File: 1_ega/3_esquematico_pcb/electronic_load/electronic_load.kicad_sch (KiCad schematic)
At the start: 43 parts, among them J1 Encoder, J10 VCC, J11 LOAD, J12 FAN, J13 RTC_I2C, J2 LCD_I2C, J3 GND, J4 MOS_GATE, J5 Isense, J6 Vload_LPF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

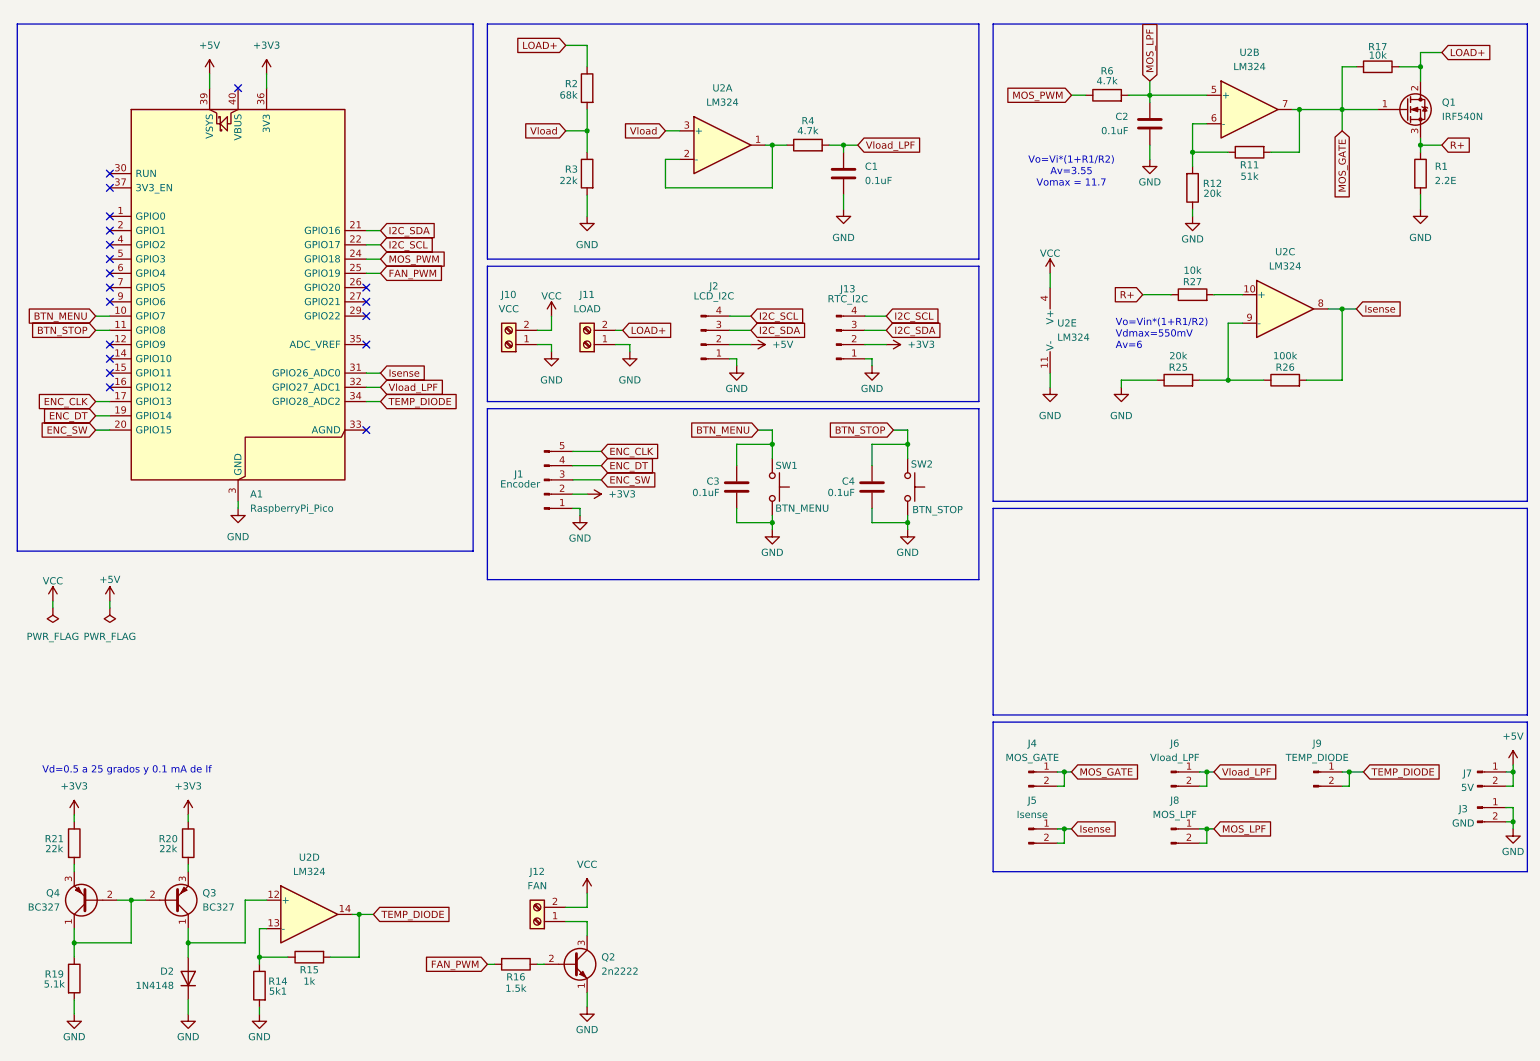
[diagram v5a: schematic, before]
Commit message: test version of i2c_guard
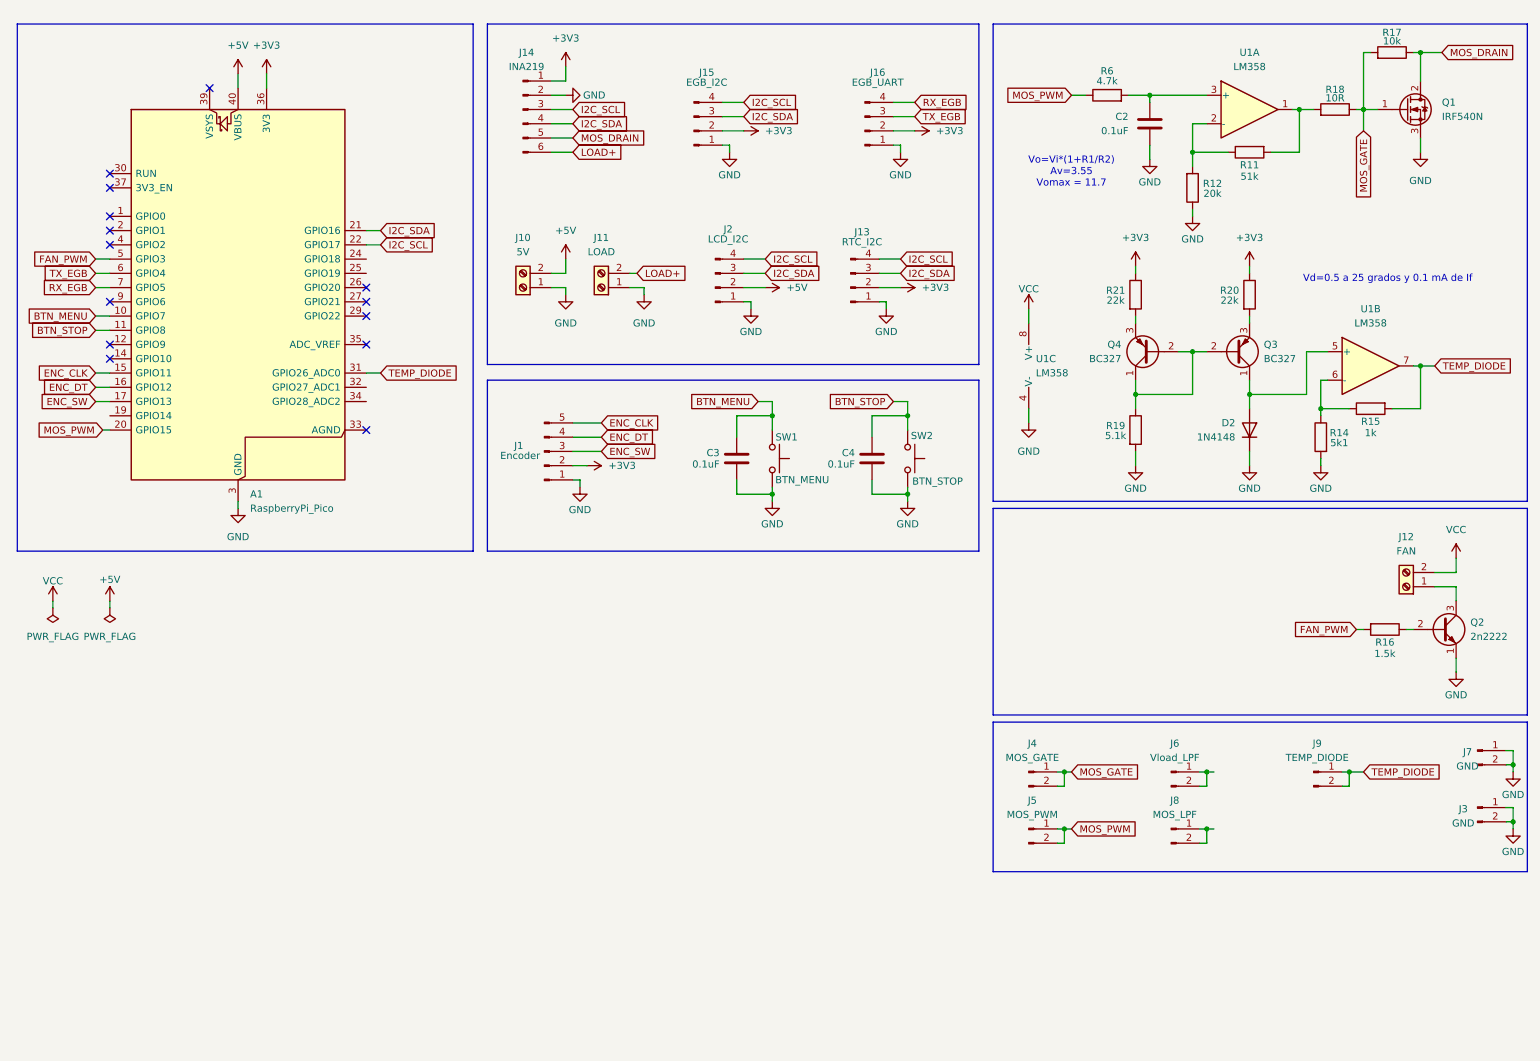
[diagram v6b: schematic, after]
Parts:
- removed C1: 0.1uF, Capacitor_THT:C_Disc_D3.4mm_W2.1mm_P2.50mm, symbol Device:C
- removed R1: 2.2E, Resistor_THT:R_Axial_Power_L25.0mm_W9.0mm_P27.94mm, symbol Device:R
- removed R2: 68k, Resistor_THT:R_Axial_DIN0207_L6.3mm_D2.5mm_P10.16mm_Horizontal, symbol Device:R
- removed R25: 20k, Resistor_THT:R_Axial_DIN0207_L6.3mm_D2.5mm_P10.16mm_Horizontal, symbol Device:R
- removed R26: 100k, Resistor_THT:R_Axial_DIN0207_L6.3mm_D2.5mm_P10.16mm_Horizontal, symbol Device:R
- removed R27: 10k, Resistor_THT:R_Axial_DIN0207_L6.3mm_D2.5mm_P10.16mm_Horizontal, symbol Device:R
- removed R3: 22k, Resistor_THT:R_Axial_DIN0207_L6.3mm_D2.5mm_P10.16mm_Horizontal, symbol Device:R
- removed R4: 4.7k, Resistor_THT:R_Axial_DIN0207_L6.3mm_D2.5mm_P10.16mm_Horizontal, symbol Device:R
- removed U2: LM324, symbol Amplifier_Operational:LM324
- added J14: INA219, Connector_PinSocket_2.54mm:PinSocket_1x06_P2.54mm_Vertical, symbol Connector:Conn_01x06_Pin
- added J15: EGB_I2C, Connector_PinSocket_2.54mm:PinSocket_1x04_P2.54mm_Vertical, symbol Connector:Conn_01x04_Pin
- added J16: EGB_UART, Connector_PinSocket_2.54mm:PinSocket_1x04_P2.54mm_Vertical, symbol Connector:Conn_01x04_Pin
- added R18: 10R, Resistor_THT:R_Axial_DIN0207_L6.3mm_D2.5mm_P10.16mm_Horizontal, symbol Device:R
- added U1: LM358, Package_DIP:DIP-8_W7.62mm_Socket_LongPads, symbol Amplifier_Operational:LM358
- J10: value VCC -> 5V
- J5: value Isense -> MOS_PWM
- J7: value 5V -> GND
- Q3, Q4: footprint Package_TO_SOT_THT:TO-92_Inline -> Package_TO_SOT_THT:TO-92_Inline_Wide
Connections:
- net R+ is gone; now on net GND: Q1.3 (S)
- net +3V3: now also J14.1 (Pin_1), J15.2 (Pin_2), J16.2 (Pin_2)
- net +5V: now also A1.40 (VBUS), J10.2 (Pin_2); no longer A1.39 (VSYS), J7.1 (Pin_1), J7.2 (Pin_2)
- net ENC_CLK: now also A1.15 (GPIO11); no longer A1.17 (GPIO13)
- net ENC_DT: now also A1.16 (GPIO12); no longer A1.19 (GPIO14)
- net ENC_SW: now also A1.17 (GPIO13); no longer A1.20 (GPIO15)
- net FAN_PWM: now also A1.5 (GPIO3); no longer A1.25 (GPIO19)
- net GND: now also J7.1 (Pin_1), J7.2 (Pin_2), J14.2 (Pin_2), J15.1 (Pin_1), J16.1 (Pin_1), U1.4 (V-)
- net I2C_SCL: now also J14.3 (Pin_3), J15.4 (Pin_4)
- net I2C_SDA: now also J14.4 (Pin_4), J15.3 (Pin_3)
- net LOAD+: now also J14.6 (Pin_6); no longer Q1.2 (D), R17.1
- net MOS_GATE: now also R18.1; no longer R11.2
- net MOS_PWM: now also A1.20 (GPIO15), J5.1 (Pin_1), J5.2 (Pin_2); no longer A1.24 (GPIO18)
- net TEMP_DIODE: now also A1.31 (GPIO26_ADC0), U1.7; no longer A1.34 (GPIO28_ADC2)
- net VCC: now also U1.8 (V+); no longer J10.2 (Pin_2)
- net at R11.1, R12.2: now also U1.2 (-)
- net at R14.1, R15.1: now also U1.6 (-)
- net at D2.2 (A), Q3.1 (C): now also U1.5 (+)
- net TX_EGB: now reaches A1.6 (GPIO4)
- net TX_EGB: now also J16.3 (Pin_3)
- net RX_EGB: now reaches A1.7 (GPIO5)
- net RX_EGB: now also J16.4 (Pin_4)
- removed net Isense: A1.31 (GPIO26_ADC0), J5.1 (Pin_1), J5.2 (Pin_2)
- net MOS_LPF: no longer names the net of C2.1, R6.2
- net MOS_LPF: now also U1.3 (+); no longer J8.1 (Pin_1), J8.2 (Pin_2)
- net Vload_LPF: no longer names the net of J6.1 (Pin_1), J6.2 (Pin_2)
- net Vload_LPF: no longer A1.32 (GPIO27_ADC1)
- new net: R11.2, R18.2, U1.1
- new net: J8.1 (Pin_1), J8.2 (Pin_2)
- new net MOS_DRAIN: J14.5 (Pin_5), Q1.2 (D), R17.1
- no-connect marks 19 -> 14
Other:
- note removed: "Vo=Vin*(1+R1/R2) Vdmax=550mV Av=6"
- moved on the sheet: C3, C4, D2, J1, J10, J11, J12, J13, J2, J7, Q2, Q3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

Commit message: feat: schematic and pcb full v1
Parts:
- removed J12: FAN, TerminalBlock_Phoenix:TerminalBlock_Phoenix_MKDS-1,5-2-5.08_1x02_P5.08mm_Horizontal, symbol Connector:Screw_Terminal_01x02
- removed J13: RTC_I2C, Connector_PinSocket_2.54mm:PinSocket_1x04_P2.54mm_Vertical, symbol Connector:Conn_01x04_Pin
- removed J15: EGB_I2C, Connector_PinSocket_2.54mm:PinSocket_1x04_P2.54mm_Vertical, symbol Connector:Conn_01x04_Pin
- removed J16: EGB_UART, Connector_PinSocket_2.54mm:PinSocket_1x04_P2.54mm_Vertical, symbol Connector:Conn_01x04_Pin
- removed J2: LCD_I2C, Connector_PinSocket_2.54mm:PinSocket_1x04_P2.54mm_Vertical, symbol Connector:Conn_01x04_Pin
- removed Q2: 2n2222, Package_TO_SOT_THT:TO-92L_Inline_Wide, symbol Transistor_BJT:2N2219
- removed R16: 1.5k, Resistor_THT:R_Axial_DIN0207_L6.3mm_D2.5mm_P10.16mm_Horizontal, symbol Device:R
- added C1: 100uF, Capacitor_THT:CP_Radial_D6.3mm_P2.50mm, symbol Device:C_Polarized
- added C5: 10nF, Capacitor_THT:C_Disc_D3.4mm_W2.1mm_P2.50mm, symbol Device:C
- added C6: 470uF, Capacitor_THT:CP_Radial_D6.3mm_P2.50mm, symbol Device:C_Polarized
- added D1: 1N5819, Diode_THT:D_DO-41_SOD81_P10.16mm_Horizontal, symbol Diode:1N5819
- added J15: VCC, TerminalBlock_Phoenix:TerminalBlock_Phoenix_MKDS-1,5-2-5.08_1x02_P5.08mm_Horizontal, symbol Connector:Screw_Terminal_01x02
- added J16: LCD_I2C, Connector_PinHeader_2.54mm:PinHeader_1x02_P2.54mm_Vertical, symbol Connector:Conn_01x02_Pin
- added J17: EGB_I2C, Connector_PinSocket_2.54mm:PinSocket_1x03_P2.54mm_Vertical, symbol Connector:Conn_01x03_Pin
- added J18: EGB_UART, Connector_PinSocket_2.54mm:PinSocket_1x03_P2.54mm_Vertical, symbol Connector:Conn_01x03_Pin
- added J2: RTC_I2C, Connector_PinSocket_2.54mm:PinSocket_1x06_P2.54mm_Vertical, symbol Connector:Conn_01x06_Pin
- added L1: 170uH, Inductor_THT:L_Radial_D10.5mm_P5.00mm_Abacron_AISR-01, symbol Device:L_Iron_Small
- added R22: 0.22R, Resistor_THT:R_Axial_DIN0207_L6.3mm_D2.5mm_P10.16mm_Horizontal, symbol Device:R
- added R23: 200R, Resistor_THT:R_Axial_DIN0207_L6.3mm_D2.5mm_P10.16mm_Horizontal, symbol Device:R
- added R24: 47k, Resistor_THT:R_Axial_DIN0207_L6.3mm_D2.5mm_P10.16mm_Horizontal, symbol Device:R
- added R25: 3.3k, Resistor_THT:R_Axial_DIN0207_L6.3mm_D2.5mm_P10.16mm_Horizontal, symbol Device:R
- added U2: MC34063AD, Package_SO:SOIC-8_3.9x4.9mm_P1.27mm, symbol Regulator_Switching:MC34063AD
- A1: footprint Module:RaspberryPi_Pico_Common_THT -> electronic_load:RaspberryPi_Pico_2_THT
- J1: footprint Connector_PinSocket_2.54mm:PinSocket_1x05_P2.54mm_Vertical -> Connector_PinHeader_2.54mm:PinHeader_1x05_P2.54mm_Vertical
- J14: footprint Connector_PinSocket_2.54mm:PinSocket_1x06_P2.54mm_Vertical -> electronic_load:INA219
- J3, J4, J5, J7, J9: footprint Connector_PinSocket_2.54mm:PinSocket_1x02_P2.54mm_Vertical -> Connector_PinHeader_2.54mm:PinHeader_1x02_P2.54mm_Vertical
- J6: value Vload_LPF -> LCD_PWR; footprint Connector_PinSocket_2.54mm:PinSocket_1x02_P2.54mm_Vertical -> Connector_PinHeader_2.54mm:PinHeader_1x02_P2.54mm_Vertical
- J8: value MOS_LPF -> MOS_VDS; footprint Connector_PinSocket_2.54mm:PinSocket_1x02_P2.54mm_Vertical -> Connector_PinHeader_2.54mm:PinHeader_1x02_P2.54mm_Vertical
- R11: value 51k -> 20k
- R12: value 20k -> 5.1k
- R14: value 5k1 -> 5.1k
- R15: value 1k -> 20k
- SW1, SW2: footprint Button_Switch_THT:SW_PUSH_6mm -> Connector_PinHeader_2.54mm:PinHeader_1x02_P2.54mm_Vertical
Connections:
- net +3V3: now also J2.5 (Pin_5)
- net +5V: now also J6.1 (Pin_1), C1.1, R22.1, U2.6 (Vin)
- net BTN_MENU: now also A1.9 (GPIO6); no longer A1.10 (GPIO7)
- net BTN_STOP: now also A1.10 (GPIO7); no longer A1.11 (GPIO8)
- net ENC_CLK: now also A1.16 (GPIO12); no longer A1.15 (GPIO11)
- net ENC_DT: now also A1.17 (GPIO13); no longer A1.16 (GPIO12)
- net ENC_SW: now also A1.19 (GPIO14); no longer A1.17 (GPIO13)
- net GND: now also J6.2 (Pin_2), C1.2, C5.1, C6.2, J15.1 (Pin_1), J17.3 (Pin_3), J18.3 (Pin_3), J2.6 (Pin_6), R25.2, U2.2 (SwE), U2.4 (GND)
- net I2C_SCL: now also J16.1 (Pin_1), J2.3 (Pin_3)
- net I2C_SDA: now also J16.2 (Pin_2), J2.4 (Pin_4)
- net MOS_DRAIN: now also J8.1 (Pin_1), J8.2 (Pin_2)
- net MOS_PWM: now also A1.24 (GPIO18); no longer A1.20 (GPIO15)
- net RX_EGB: now also J18.2 (Pin_2)
- net TEMP_DIODE: now also U1.1; no longer U1.7
- net TX_EGB: now also J18.1 (Pin_1)
- net VCC: now also C6.1, D1.1 (K), J15.2 (Pin_2), R24.2
- net at C2.1, R6.2: now also U1.5 (+); no longer U1.3 (+)
- net at R11.1, R12.2: now also U1.6 (-); no longer U1.2 (-)
- net at R11.2, R18.2: now also U1.7; no longer U1.1
- net at R14.1, R15.1: now also U1.2 (-); no longer U1.6 (-)
- net at D2.2 (A), Q3.1 (C): now also U1.3 (+); no longer U1.5 (+)
- net I2C1_SCL: now reaches A1.14 (GPIO10)
- net I2C1_SCL: now also J17.1 (Pin_1)
- net FAN_PWM: no longer names the net of A1.5 (GPIO3)
- new net: L1.1, R22.2, R23.1, U2.7 (Ipk)
- new net: D1.2 (A), L1.2, U2.1 (SwC)
- new net: R24.1, R25.1, U2.5 (Vfb)
- new net: C5.2, U2.3 (TC)
- new net: R23.2, U2.8 (DC)
- new net I2C1_SDA: A1.15 (GPIO11), J17.2 (Pin_2)
- new net RTC_32K: J2.1 (Pin_1)
- new net RTC_SQW: J2.2 (Pin_2)
- no-connect marks 14 -> 18
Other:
- note added: "Borneras"
- note added: "Fuente Boost Vout=16V"
- note added: "GPIO - Usuario"
- note added: "Op Amp (doble) Alternativa TL072"
- note added: "Perifericos I2C"
- note added: "Pines EGB"
- note added: "Raspberry Pico 2"
- note added: "Test Points"
- note added: "Vd=0.5 a 25 grados y 0.1 mA de If Vin_max=0.65v Av=5 R2/R1=4"
- note added: "Vo=Vi*(1+R2/R1) Vomax=16v Av=4.84"
- note removed: "Vd=0.5 a 25 grados y 0.1 mA de If"
- note removed: "Vo=Vi*(1+R1/R2) Av=3.55 Vomax = 11.7"
- moved on the sheet: A1, C2, C3, C4, D2, J1, J10, J11, J14, J3, J4, J5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
